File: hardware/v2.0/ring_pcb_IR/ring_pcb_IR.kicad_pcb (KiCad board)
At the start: 2 copper layers, 19.1 x 19.1 mm, 11 parts, among them Q1 Q_PNP_BEC, Q2 Q_PNP_BEC, Q3 Q_NPN_BEC, Q4 Q_NPN_BEC, Q5 Q_NPN_BEC, Q6 Q_NPN_BEC, U1 ATtiny85-20M

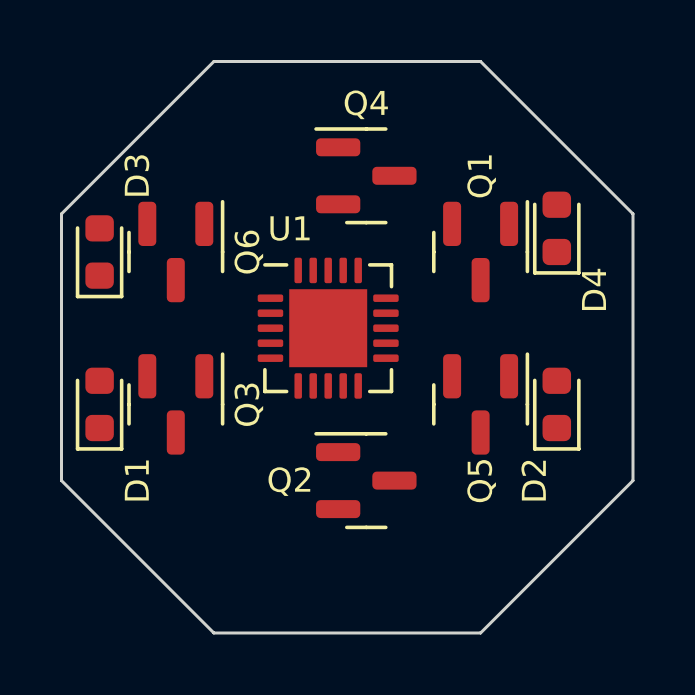
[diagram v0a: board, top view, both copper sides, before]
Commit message: Start wiring up LED driver
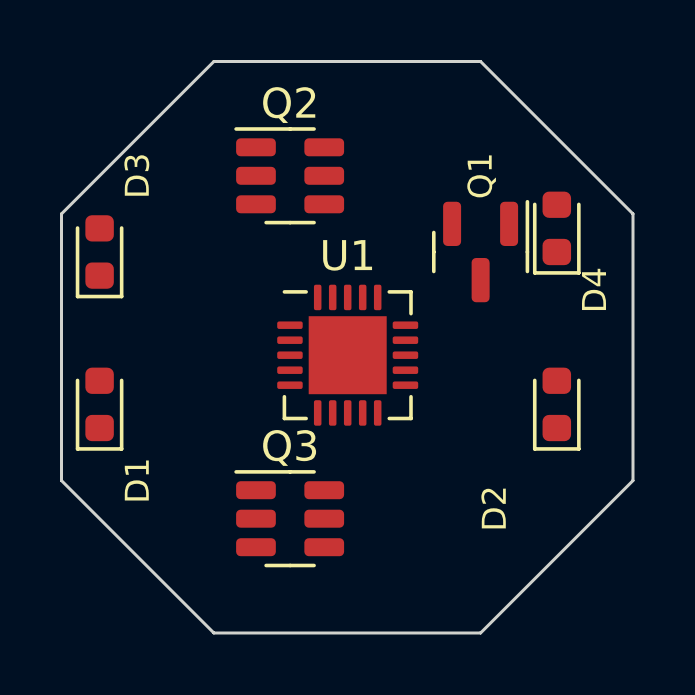
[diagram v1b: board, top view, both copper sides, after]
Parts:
- removed Q4, Q5, Q6: Q_NPN_BEC, Package_TO_SOT_SMD:SOT-23
- Q2: value Q_PNP_BEC -> Q_Dual_NPN_NPN_C2E2C1E1B1B2; footprint Package_TO_SOT_SMD:SOT-23 -> Package_TO_SOT_SMD:SOT-23-6
- Q3: value Q_NPN_BEC -> Q_Dual_NPN_NPN_C2E2C1E1B1B2; footprint Package_TO_SOT_SMD:SOT-23 -> Package_TO_SOT_SMD:SOT-23-6
- U1: value ATtiny85-20M -> ATtiny85V-10M
- moved Q2 10.5 mm to (134.6, 105.4)
- moved Q3 5.39 mm to (134.6, 116.8), turned to 0 degrees
- moved U1 1.11 mm to (136.5, 111.4)
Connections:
- D1 pad 1: unconnected-(D1-Pad1) -> Net-(D1-Pad1)
- D1 pad 2: unconnected-(D1-Pad2) -> VCC
- D2 pad 1: unconnected-(D2-Pad1) -> Net-(D2-Pad1)
- D2 pad 2: unconnected-(D2-Pad2) -> VCC
- D3 pad 1: unconnected-(D3-Pad1) -> Net-(D3-Pad1)
- D3 pad 2: unconnected-(D3-Pad2) -> VCC
- D4 pad 1: unconnected-(D4-Pad1) -> Net-(D4-Pad1)
- D4 pad 2: unconnected-(D4-Pad2) -> VCC
- Q2 pad 1: unconnected-(Q2-Pad1) -> Net-(D4-Pad1)
- Q2 pad 3: unconnected-(Q2-Pad3) -> Net-(D2-Pad1)
- Q3 pad 1: unconnected-(Q3-Pad1) -> Net-(D3-Pad1)
- Q3 pad 3: unconnected-(Q3-Pad3) -> Net-(D1-Pad1)

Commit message: Reposition parts
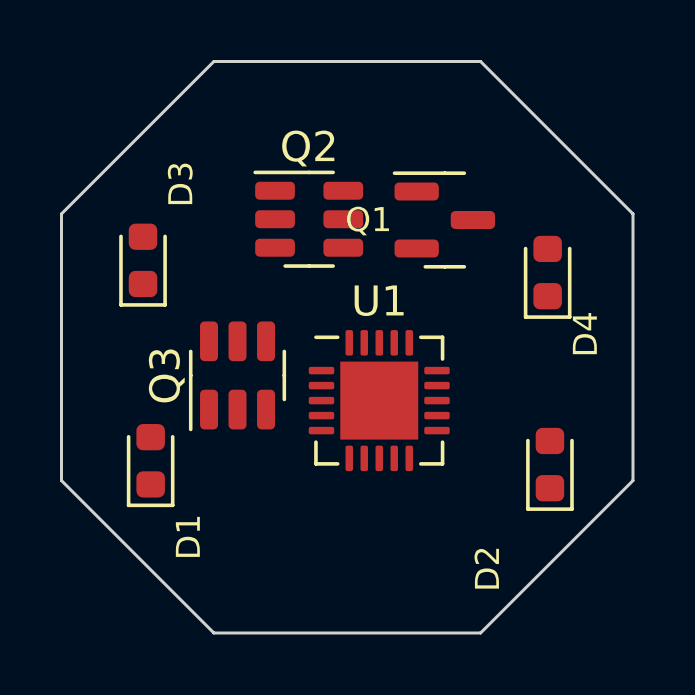
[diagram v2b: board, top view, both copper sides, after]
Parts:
- moved Q3 5.09 mm to (132.9, 112.1), turned to 90 degrees
- moved D1 2.54 mm to (130.0, 114.9)
- moved D2 2.02 mm to (143.3, 115.0)
- moved U1 1.84 mm to (137.6, 112.9)
- moved Q1 1.60 mm to (139.8, 106.9), turned to 0 degrees
- moved Q2 1.58 mm to (135.3, 106.9)
- moved D4 1.50 mm to (143.2, 108.6)
- moved D3 1.47 mm to (129.7, 108.2)
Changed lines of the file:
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@@
   (net 33 "unconnected-(Q3-Pad4)")
   (footprint "Package_TO_SOT_SMD:SOT-23" (layer "F.Cu")
-    (at 140.97 107.95 -90)
+    (at 139.7762 106.8832)
     (descr "SOT, 3 Pin (https://www.jedec.org/system/files/docs/to-236h.pdf variant AB), generated with kicad-footprint-generator ipc_gullwing_generator.py")
     (tags "SOT TO_SOT_SMD")
@@
     (property "Sheetname" "")
     (attr smd)
-    (fp_text reference "Q1" (at -2.54 0 90) (layer "F.SilkS")
-      (effects (font (size 0.8 0.8) (thickness 0.2)))
-    )
-    (fp_text value "Q_PNP_BEC" (at 0 2.4 90) (layer "F.Fab")
-      (effects (font (size 1 1) (thickness 0.15)))
-    )
-    (fp_text user "${REFERENCE}" (at 0 0 90) (layer "F.Fab")
+    (fp_text reference "Q1" (at -2.54 0) (layer "F.SilkS")
+      (effects (font (size 0.8 0.8) (thickness 0.2)))
+    )
+    (fp_text value "Q_PNP_BEC" (at 0 2.4) (layer "F.Fab")
+      (effects (font (size 1 1) (thickness 0.15)))
+    )
+    (fp_text user "${REFERENCE}" (at 0 0) (layer "F.Fab")
       (effects (font (size 0.8 0.8) (thickness 0.2)))
     )
@@
     (fp_line (start -0.65 -1.125) (end -0.325 -1.45) (layer "F.Fab") (width 0.1))
     (fp_line (start -0.325 -1.45) (end 0.65 -1.45) (layer "F.Fab") (width 0.1))
-    (pad "1" smd roundrect locked (at -0.9375 -0.95 270) (size 1.475 0.6) (layers "F.Cu" "F.Paste" "F.Mask") (roundrect_rratio 0.25)
+    (pad "1" smd roundrect locked (at -0.9375 -0.95) (size 1.475 0.6) (layers "F.Cu" "F.Paste" "F.Mask") (roundrect_rratio 0.25)
       (net 21 "unconnected-(Q1-Pad1)") (pinfunction "B") (pintype "input"))
-    (pad "2" smd roundrect locked (at -0.9375 0.95 270) (size 1.475 0.6) (layers "F.Cu" "F.Paste" "F.Mask") (roundrect_rratio 0.25)
+    (pad "2" smd roundrect locked (at -0.9375 0.95) (size 1.475 0.6) (layers "F.Cu" "F.Paste" "F.Mask") (roundrect_rratio 0.25)
       (net 22 "unconnected-(Q1-Pad2)") (pinfunction "E") (pintype "passive"))
-    (pad "3" smd roundrect locked (at 0.9375 0 270) (size 1.475 0.6) (layers "F.Cu" "F.Paste" "F.Mask") (roundrect_rratio 0.25)
+    (pad "3" smd roundrect locked (at 0.9375 0) (size 1.475 0.6) (layers "F.Cu" "F.Paste" "F.Mask") (roundrect_rratio 0.25)
       (net 23 "unconnected-(Q1-Pad3)") (pinfunction "C") (pintype "passive"))
     (model "${KICAD6_3DMODEL_DIR}/Package_TO_SOT_SMD.3dshapes/SOT-23.wrl"
@@
   )
   (footprint "LED_SMD:LED_0603_1608Metric" (layer "F.Cu")
-    (at 128.27 107.95 90)
+    (at 129.7178 108.2294 90)
     (descr "LED SMD 0603 (1608 Metric), square (rectangular) end terminal, IPC_7351 nominal, (Body size source: http://www.tortai-tech.com/upload/download/2011102023233369053.pdf), generated with kicad-footprint-generator")
     (tags "LED")
@@
   )
   (footprint "LED_SMD:LED_0603_1608Metric" (layer "F.Cu")
-    (at 128.27 113.03 90)
+    (at 129.9718 114.9096 90)
     (descr "LED SMD 0603 (1608 Metric), square (rectangular) end terminal, IPC_7351 nominal, (Body size source: http://www.tortai-tech.com/upload/download/2011102023233369053.pdf), generated with kicad-footprint-generator")
     (tags "LED")
@@
   )
   (footprint "LED_SMD:LED_0603_1608Metric" (layer "F.Cu")
-    (at 143.51 107.1625 90)
+    (at 143.2052 108.6357 90)
     (descr "LED SMD 0603 (1608 Metric), square (rectangular) end terminal, IPC_7351 nominal, (Body size source: http://www.tortai-tech.com/upload/download/2011102023233369053.pdf), generated with kicad-footprint-generator")
     (tags "LED")
@@
   )
   (footprint "Package_DFN_QFN:QFN-20-1EP_4x4mm_P0.5mm_EP2.6x2.6mm" (layer "F.Cu")
-    (at 136.54 111.39)
+    (at 137.5918 112.903)
     (descr "QFN, 20 Pin (http://ww1.microchip.com/downloads/en/DeviceDoc/doc2535.pdf#page=164), generated with kicad-footprint-generator ipc_noLead_generator.py")
     (tags "QFN NoLead")
@@
   )
   (footprint "Package_TO_SOT_SMD:SOT-23-6" (layer "F.Cu")
-    (at 134.62 105.41)
+    (at 135.255 106.8578)
     (descr "SOT, 6 Pin (https://www.jedec.org/sites/default/files/docs/Mo-178c.PDF variant AB), generated with kicad-footprint-generator ipc_gullwing_generator.py")
     (tags "SOT TO_SOT_SMD")
@@
   )
   (footprint "LED_SMD:LED_0603_1608Metric" (layer "F.Cu")
-    (at 143.51 113.03 90)
+    (at 143.2814 115.0366 90)
     (descr "LED SMD 0603 (1608 Metric), square (rectangular) end terminal, IPC_7351 nominal, (Body size source: http://www.tortai-tech.com/upload/download/2011102023233369053.pdf), generated with kicad-footprint-generator")
     (tags "LED")
@@
   )
   (footprint "Package_TO_SOT_SMD:SOT-23-6" (layer "F.Cu")
-    (at 134.62 116.84)
+    (at 132.8674 112.0648 90)
     (descr "SOT, 6 Pin (https://www.jedec.org/sites/default/files/docs/Mo-178c.PDF variant AB), generated with kicad-footprint-generator ipc_gullwing_generator.py")
     (tags "SOT TO_SOT_SMD")
@@
     (property "Sheetname" "")
     (attr smd)
-    (fp_text reference "Q3" (at 0 -2.4) (layer "F.SilkS")
-      (effects (font (size 1 1) (thickness 0.15)))
-    )
-    (fp_text value "Q_Dual_NPN_NPN_C2E2C1E1B1B2" (at 0 2.4) (layer "F.Fab")
-      (effects (font (size 1 1) (thickness 0.15)))
-    )
-    (fp_text user "${REFERENCE}" (at 0 0) (layer "F.Fab")
+    (fp_text reference "Q3" (at 0 -2.4 90) (layer "F.SilkS")
+      (effects (font (size 1 1) (thickness 0.15)))
+    )
+    (fp_text value "Q_Dual_NPN_NPN_C2E2C1E1B1B2" (at 0 2.4 90) (layer "F.Fab")
+      (effects (font (size 1 1) (thickness 0.15)))
+    )
+    (fp_text user "${REFERENCE}" (at 0 0 90) (layer "F.Fab")
       (effects (font (size 0.4 0.4) (thickness 0.06)))
     )
@@
     (fp_line (start -0.8 1.45) (end -0.8 -1.05) (layer "F.Fab") (width 0.1))
     (fp_line (start -0.8 -1.05) (end -0.4 -1.45) (layer "F.Fab") (width 0.1))
-    (pad "1" smd roundrect locked (at -1.1375 -0.95) (size 1.325 0.6) (layers "F.Cu" "F.Paste" "F.Mask") (roundrect_rratio 0.25)
+    (pad "1" smd roundrect locked (at -1.1375 -0.95 90) (size 1.325 0.6) (layers "F.Cu" "F.Paste" "F.Mask") (roundrect_rratio 0.25)
       (net 29 "Net-(D3-Pad1)") (pinfunction "C2") (pintype "passive"))
-    (pad "2" smd roundrect locked (at -1.1375 0) (size 1.325 0.6) (layers "F.Cu" "F.Paste" "F.Mask") (roundrect_rratio 0.25)
+    (pad "2" smd roundrect locked (at -1.1375 0 90) (size 1.325 0.6) (layers "F.Cu" "F.Paste" "F.Mask") (roundrect_rratio 0.25)
       (net 28 "unconnected-(Q3-Pad2)") (pinfunction "E2") (pintype "passive"))
-    (pad "3" smd roundrect locked (at -1.1375 0.95) (size 1.325 0.6) (layers "F.Cu" "F.Paste" "F.Mask") (roundrect_rratio 0.25)
+    (pad "3" smd roundrect locked (at -1.1375 0.95 90) (size 1.325 0.6) (layers "F.Cu" "F.Paste" "F.Mask") (roundrect_rratio 0.25)
       (net 24 "Net-(D1-Pad1)") (pinfunction "C1") (pintype "passive"))
-    (pad "4" smd roundrect locked (at 1.1375 0.95) (size 1.325 0.6) (layers "F.Cu" "F.Paste" "F.Mask") (roundrect_rratio 0.25)
+    (pad "4" smd roundrect locked (at 1.1375 0.95 90) (size 1.325 0.6) (layers "F.Cu" "F.Paste" "F.Mask") (roundrect_rratio 0.25)
       (net 33 "unconnected-(Q3-Pad4)") (pinfunction "E1") (pintype "passive"))
-    (pad "5" smd roundrect locked (at 1.1375 0) (size 1.325 0.6) (layers "F.Cu" "F.Paste" "F.Mask") (roundrect_rratio 0.25)
+    (pad "5" smd roundrect locked (at 1.1375 0 90) (size 1.325 0.6) (layers "F.Cu" "F.Paste" "F.Mask") (roundrect_rratio 0.25)
       (net 32 "Net-(Q2-Pad5)") (pinfunction "B1") (pintype "input"))
-    (pad "6" smd roundrect locked (at 1.1375 -0.95) (size 1.325 0.6) (layers "F.Cu" "F.Paste" "F.Mask") (roundrect_rratio 0.25)
+    (pad "6" smd roundrect locked (at 1.1375 -0.95 90) (size 1.325 0.6) (layers "F.Cu" "F.Paste" "F.Mask") (roundrect_rratio 0.25)
       (net 32 "Net-(Q2-Pad5)") (pinfunction "B2") (pintype "input"))
     (model "${KICAD6_3DMODEL_DIR}/Package_TO_SOT_SMD.3dshapes/SOT-23-6.wrl"

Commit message: Add IR components
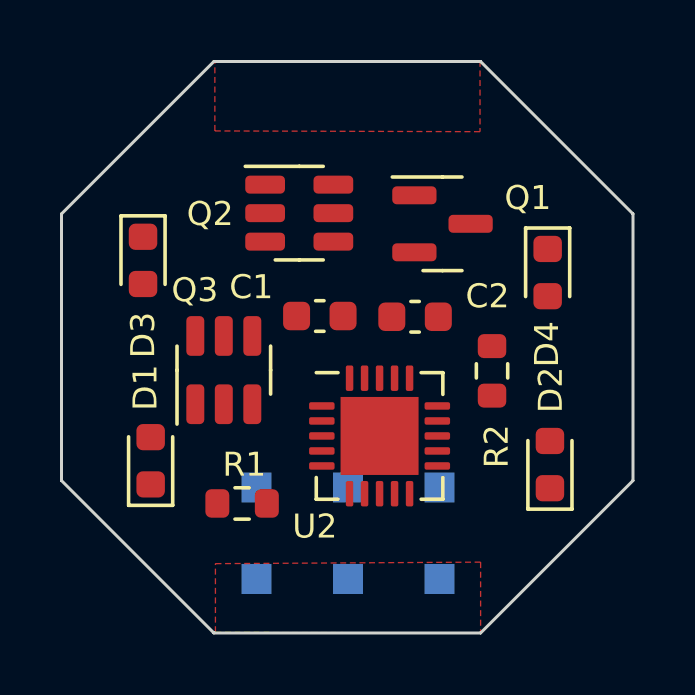
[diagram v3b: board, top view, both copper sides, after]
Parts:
- removed U1: ATtiny85V-10M, Package_DFN_QFN:QFN-20-1EP_4x4mm_P0.5mm_EP2.6x2.6mm
- added C1: 100n, Capacitor_SMD:C_0603_1608Metric, F.Cu at (135.6, 110.1)
- added C2: 100u, Capacitor_SMD:C_0603_1608Metric, F.Cu at (138.8, 110.1)
- added R1: 1k, Resistor_SMD:R_0603_1608Metric, F.Cu at (133.0, 116.3)
- added R2: 200, Resistor_SMD:R_0603_1608Metric, F.Cu at (141.4, 111.9)
- added TP1: TestPoint, TestPoint:TestPoint_Pad_1.0x1.0mm, B.Cu at (139.6, 115.8)
- added TP2: TestPoint, TestPoint:TestPoint_Pad_1.0x1.0mm, B.Cu at (139.6, 118.8)
- added TP3: TestPoint, TestPoint:TestPoint_Pad_1.0x1.0mm, B.Cu at (136.6, 115.8)
- added TP4: TestPoint, TestPoint:TestPoint_Pad_1.0x1.0mm, B.Cu at (136.6, 118.8)
- added TP5: TestPoint, TestPoint:TestPoint_Pad_1.0x1.0mm, B.Cu at (133.5, 115.8)
- added TP6: TestPoint, TestPoint:TestPoint_Pad_1.0x1.0mm, B.Cu at (133.5, 118.8)
- added U2: ATtiny85-20M, Package_DFN_QFN:QFN-20-1EP_4x4mm_P0.5mm_EP2.6x2.6mm, F.Cu at (137.6, 114.1)
- moved Q3 0.49 mm to (132.4, 111.9)
- moved Q2 0.39 mm to (134.9, 106.7)
- moved Q1 0.15 mm to (139.7, 107.0)
- turned D3 to -90 degrees
- turned D4 to -90 degrees
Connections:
- Q1 pad 1: unconnected-(Q1-Pad1) -> Net-(Q1-B)
- Q1 pad 2: unconnected-(Q1-Pad2) -> Net-(Q1-E)
- Q2 pad 2: unconnected-(Q2-Pad2) -> GND
- Q2 pad 4: unconnected-(Q2-Pad4) -> GND
- Q2 pad 5: Net-(Q2-Pad5) -> Net-(Q1-E)
- Q2 pad 6: Net-(Q2-Pad5) -> Net-(Q1-E)
- Q3 pad 2: unconnected-(Q3-Pad2) -> GND
- Q3 pad 4: unconnected-(Q3-Pad4) -> GND
- Q3 pad 5: Net-(Q2-Pad5) -> Net-(Q1-E)
- Q3 pad 6: Net-(Q2-Pad5) -> Net-(Q1-E)
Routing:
- added copper zone on F.Cu, net GND

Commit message: Add more wiring for LED and power pads
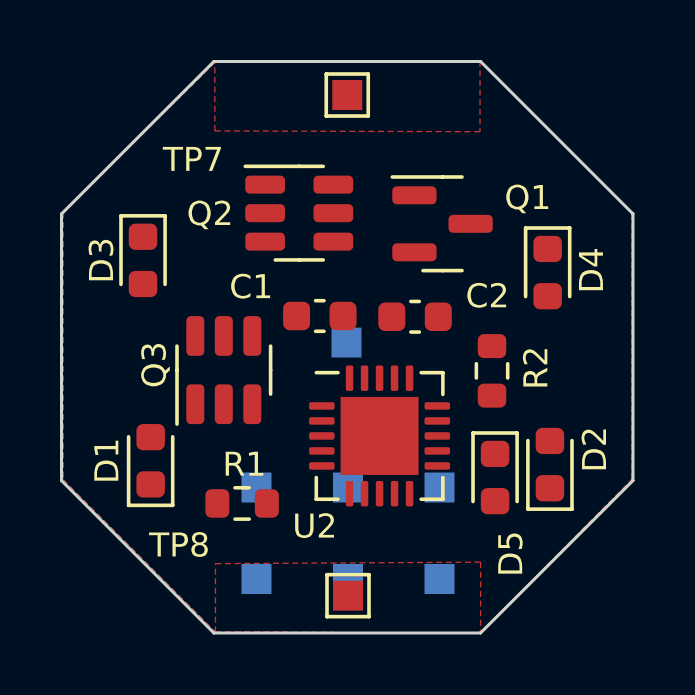
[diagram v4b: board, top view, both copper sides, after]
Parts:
- added D5: LED, LED_SMD:LED_0603_1608Metric, F.Cu at (141.5, 115.5)
- added TP7: TestPoint, TestPoint:TestPoint_Pad_1.0x1.0mm, F.Cu at (136.5, 102.7)
- added TP8: TestPoint, TestPoint:TestPoint_Pad_1.0x1.0mm, F.Cu at (136.6, 119.4)
- added TP9: TestPoint, TestPoint:TestPoint_Pad_1.0x1.0mm, B.Cu at (136.5, 111.0)
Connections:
- R1 pad 1: unconnected-(R1-Pad1) -> PB0
- R2 pad 1: unconnected-(R2-Pad1) -> Net-(D5-K)
- R2 pad 2: unconnected-(R2-Pad2) -> PB2
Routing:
- added copper zone on B.Cu, net VCC

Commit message: Route PCB
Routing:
- net Net-(Q1-B): track 0.00 -> 33.7 mm
- net VCC: track 0.00 -> 17.7 mm, vias 0 -> 4
- net Net-(D2-K): track 0.00 -> 16.1 mm
- net Net-(Q1-E): track 0.00 -> 14.3 mm
- net PB3: track 0.00 -> 12.4 mm, vias 0 -> 1
- net Net-(D4-K): track 0.00 -> 11.8 mm
- net PB2: track 0.00 -> 10.6 mm, vias 0 -> 1
- net PB0: track 0.00 -> 8.91 mm, vias 0 -> 1
- net PB5: track 0.00 -> 7.92 mm, vias 0 -> 1
- net PB1: track 0.00 -> 6.91 mm, vias 0 -> 1
- net Net-(D3-K): track 0.00 -> 6.30 mm
- net Net-(D1-K): track 0.00 -> 4.77 mm
- net PB4: track 0.00 -> 2.95 mm, vias 0 -> 1
- net Net-(D5-K): track 0.00 -> 1.99 mm

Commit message: Fix routing, squash unrouted
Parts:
- moved D5 12.5 mm to (133.3, 105.9), turned to 90 degrees
- moved Q2 9.52 mm to (143.3, 111.3), turned to 180 degrees
- moved R2 8.46 mm to (135.4, 105.9)
- moved D2 8.10 mm to (143.3, 106.9)
- moved D4 6.68 mm to (143.3, 115.3)
- moved Q3 1.72 mm to (130.8, 111.3), turned to 0 degrees
- moved Q1 1.52 mm to (138.4, 106.2), turned to 90 degrees
- moved D3 1.34 mm to (130.0, 106.9), turned to 90 degrees
- moved R1 1.03 mm to (132.3, 115.6), turned to 90 degrees
- moved D1 0.76 mm to (130.3, 115.6), turned to -90 degrees
- moved C1 0.65 mm to (135.4, 109.5)
- moved C2 0.63 mm to (138.8, 109.5)
- moved U2 0.35 mm to (137.4, 113.8)
- moved TP9 0.32 mm to (136.7, 111.3)
- moved TP8 0.25 mm to (136.7, 119.6)
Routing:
- net VCC: track 17.7 -> 37.7 mm, vias 4 -> 5
- net Net-(D2-K): track 16.1 -> 3.05 mm
- net Net-(Q1-B): track 33.7 -> 22.0 mm
- net GND: track 0.00 -> 10.3 mm, vias 0 -> 2
- net Net-(D4-K): track 11.8 -> 2.80 mm
- net PB2: track 10.6 -> 17.3 mm, vias 1 -> 2
- net PB3: track 12.4 -> 7.59 mm
- net Net-(Q1-E): track 14.3 -> 19.1 mm
- net PB0: track 8.91 -> 12.3 mm
- net PB1: track 6.91 -> 9.79 mm
- net PB4: track 2.95 -> 5.80 mm
- net PB5: track 7.92 -> 10.4 mm
- net Net-(D3-K): track 6.30 -> 4.10 mm
- net Net-(D1-K): track 4.77 -> 3.86 mm
